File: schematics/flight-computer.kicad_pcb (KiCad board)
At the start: 4 copper layers, 91.4 x 70 mm, 74 parts, among them IC1 NC7SZ04, IC2 MAX14787E, IC3 MAX14787E, J1 BATT, J2 SERIAL, J3 BLACKBOX, J4 BMI-S-201, P1 SWD_TC, P2 GPS, P3 TLM, U1 MAX604, U2 MAX604, U3 STM32F405RGT6, U5 MS5611-01BA, U6 ICM-20948, U7 Si4463, U8 MAX-M8Q, U9 CDCLVC1103PW, Y1 TCXO

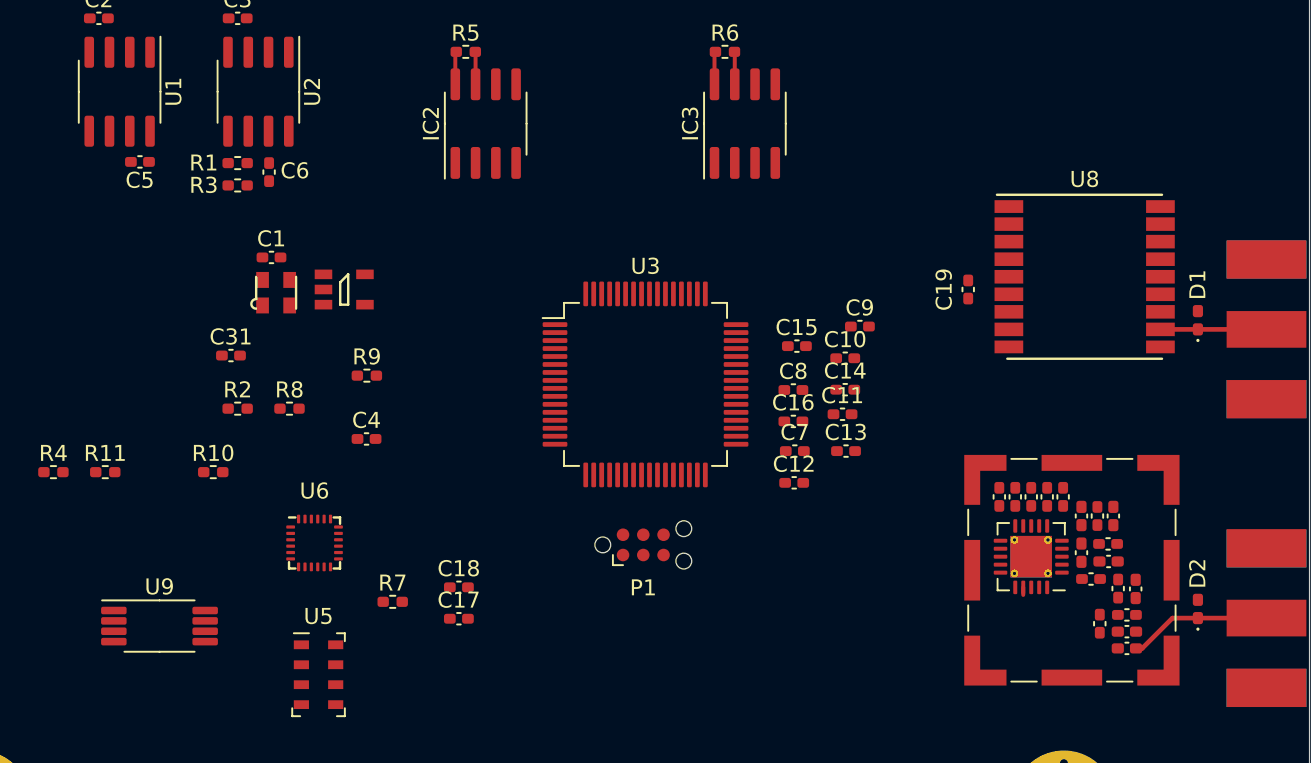
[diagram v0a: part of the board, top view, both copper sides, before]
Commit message: Migrate remaining symbols to local library
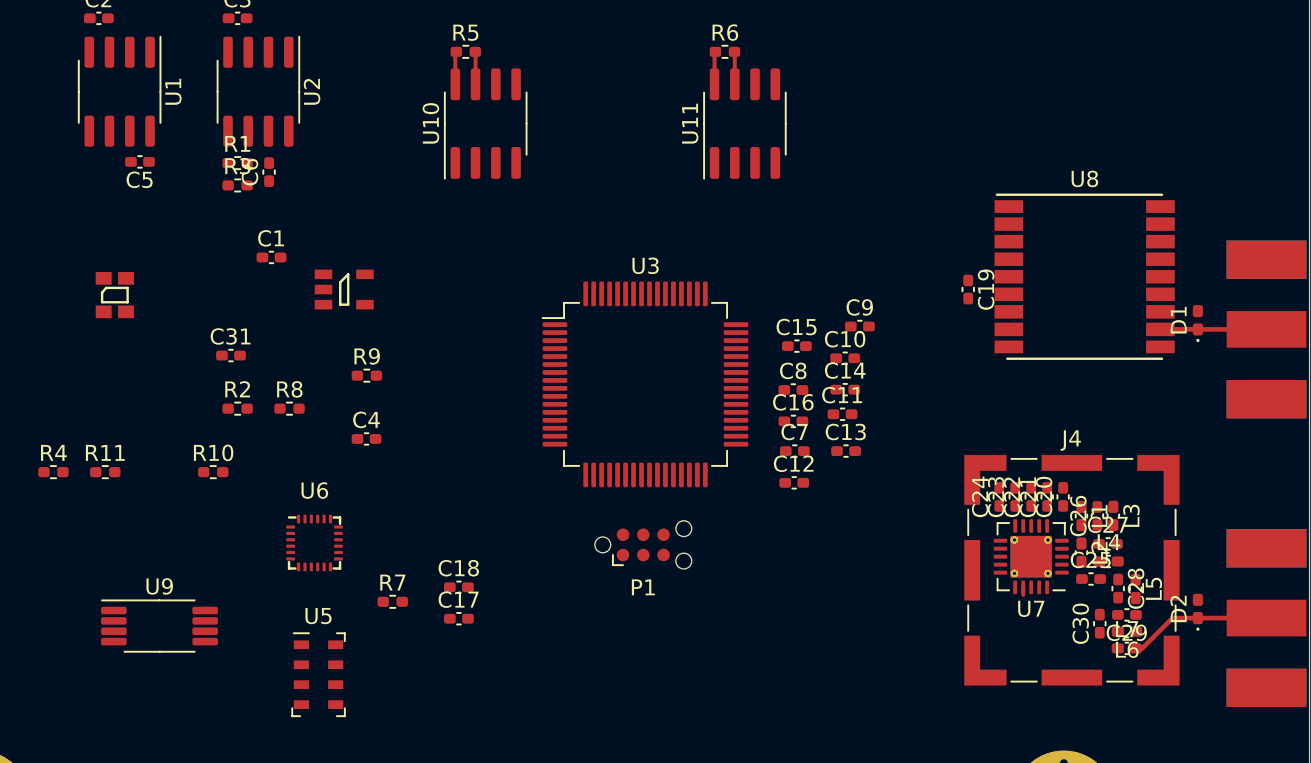
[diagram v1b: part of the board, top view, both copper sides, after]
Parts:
- C1, C10, C11, C12, C13, C14, C15, C16, C17, C18, C19, C2, C20, C21, C22, C23, C24, C25, C26, C27, C28, C29, C3, C30, C31, C4, C5, C6, C7, C8, C9: footprint Strix:C_0402_1005Metric_Pad0.74x0.62mm_HandSolder -> Strix:C_0402
- D1, D2: footprint Strix:D_0402_1005Metric_Pad0.77x0.64mm_HandSolder -> Strix:D_0402
- H1, H2, H3, H4: footprint Strix:MountingHole_3.2mm_M3_Pad_Via -> Strix:MountingHole_Pad
- J1: footprint Strix:Molex_Nano-Fit_105313-xx03_1x03_P2.50mm_Horizontal -> Strix:Molex_Nano-Fit_105313-1103
- J2: footprint Strix:Molex_Nano-Fit_105314-xx06_2x03_P2.50mm_Horizontal -> Strix:Molex_Nano-Fit_105314-1106
- J3: footprint Strix:Molex_Nano-Fit_105314-xx08_2x04_P2.50mm_Horizontal -> Strix:Molex_Nano-Fit_105314-1108
- J4: footprint Strix:Laird_Technologies_BMI-S-201-F_13.66x12.70mm -> Strix:BMI-S-201
- L1, L2, L3, L4, L5, L6, L7: footprint Strix:L_0402_1005Metric_Pad0.77x0.64mm_HandSolder -> Strix:L_0402
- P1: footprint Strix:Tag-Connect_TC2030-IDC-NL_2x03_P1.27mm_Vertical -> Strix:SWD_TC
- R1, R10, R11, R2, R3, R4, R5, R6, R7, R8, R9: footprint Strix:R_0402_1005Metric_Pad0.72x0.64mm_HandSolder -> Strix:R_0402
- U1, U2: footprint Strix:SOIC-8_3.9x4.9mm_P1.27mm -> Strix:MAX604
- U3: footprint Strix:LQFP-64_10x10mm_P0.5mm -> Strix:STM32F405RGT6
- U5: footprint Strix:LGA-8_3x5mm_P1.25mm -> Strix:MS5611-01BA
- U6: footprint Strix:InvenSense_QFN-24_3x3mm_P0.4mm -> Strix:ICM-20948
- U7: footprint Strix:QFN-20-1EP_4x4mm_P0.5mm_EP2.6x2.6mm_ThermalVias -> Strix:Si4463
- U9: footprint Strix:TSSOP-8_4.4x3mm_P0.65mm -> Strix:CDCLVC1103PW
- Y1: value TCXO -> LFTCXO068373; footprint cusf:XTAL-25x20 -> Strix:LFTCXO068373
- moved Y1 10.1 mm to (180.5, 103.2), turned to 0 degrees
- renumbered IC2 to U10, IC3 to U11, IC1 to U12
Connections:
- Y1 pad 1: (no net) -> GND

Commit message: Migrate to KiCad 6
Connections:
- net /BARO_~CS renamed /BARO_~{CS}
- net /GPS_~RESET renamed /GPS_~{RESET}
- net /RADIO_~CS renamed /RADIO_~{CS}
- net /RADIO_~INT renamed /RADIO_~{INT}
- net /~RST renamed /~{RST}
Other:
- net class 50ohm removed
- net class Default removed

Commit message: Complete revision 1 schematic
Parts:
- removed C29, C30: 3p3, Strix:C_0402
- removed C31: 10n, Strix:C_0402
- removed J4: BMI-S-201, Strix:BMI-S-201
- removed P3: TLM, Strix:SMA-EDGE
- removed R10: 10, Strix:R_0402
- removed R11: 10k, Strix:R_0402
- removed R7: 100k, Strix:R_0402
- removed R8, R9: 510k, Strix:R_0402
- removed U10, U11: MAX14787E, Strix:MAX14787E
- removed U12: NC7SZ04, cusf:SOT-23-5
- removed U3: STM32F405RGT6, Strix:STM32F405RGT6
- removed U5: MS5611-01BA, Strix:MS5611-01BA
- removed Y1: LFTCXO068373, Strix:LFTCXO068373
- added U4: MS5611-01BA, Strix:MS5611-01BA, F.Cu at (308.0, 136.0)
- C1: value 100n -> 1µ
- C14: value 2µ2 -> 1u
- C15: value 2µ2 -> 2u2
- C17: value 100n -> 220p
- C18: value 100n -> 100p
- C19: value 100n -> 3p
- C2: value 10u -> 4µ7
- C20: value 1u -> 5p1
- C21: value 2u2 -> 1p2
- C22: value 100n -> 6n8
- C23: value 220p -> 3p3
- C24: value 100p -> 3p3
- C25: value 3p -> 10u
- C26: value 5p1 -> 10u
- C27: value 1p2 -> 10u
- C28: value 6n8 -> 10u
- C3, C5, C6: value 10u -> 100n
- C4: value 1n -> 100n
- C7: value 1µ -> 100n
- C8: value 4µ7 -> 2µ2
- C9: value 100n -> 2µ2
- J2: value SERIAL -> BLACKBOX; footprint Strix:Molex_Nano-Fit_105314-1106 -> Strix:Molex_Nano-Fit_105314-1108
- J3: value BLACKBOX -> BMI-S-201; footprint Strix:Molex_Nano-Fit_105314-1108 -> Strix:BMI-S-201
- P1: value SWD_TC -> GPS; footprint Strix:SWD_TC -> Strix:SMA-EDGE
- P2: value GPS -> TLM
- R1: value 200k -> 120
- R2: value 10 -> 100k
- R3: value 100k -> 10k
- R5: value 120 -> 200k
- R6: value 120 -> 100k
- U1: value MAX604 -> STM32F405RGT6; footprint Strix:MAX604 -> Strix:STM32F405RGT6
- U2: value MAX604 -> MAX14787E; footprint Strix:MAX604 -> Strix:MAX14787E
- U6: value ICM-20948 -> Si4463; footprint Strix:ICM-20948 -> Strix:Si4463
- U7: value Si4463 -> MAX-M8Q; footprint Strix:Si4463 -> Strix:MAX-M8Q
- U8: value MAX-M8Q -> MAX604; footprint Strix:MAX-M8Q -> Strix:MAX604
- U9: value CDCLVC1103PW -> MAX604; footprint Strix:CDCLVC1103PW -> Strix:MAX604
- moved H4 125.9 mm to (262.0, 168.0)
- moved H3 124.5 mm to (328.0, 168.0)
- moved U1 122.6 mm to (295.0, 135.0), turned to 0 degrees
- moved U6 117.4 mm to (310.4, 116.0)
- moved P1 114.4 mm to (323.2, 152.0), turned to -90 degrees
- moved J1 112.6 mm to (266.1, 155.5), turned to 180 degrees
- moved J3 101.8 mm to (312.0, 118.0), turned to 0 degrees
- moved U9 98.7 mm to (276.0, 158.0)
- moved H1 95.9 mm to (262.0, 102.0)
- moved H2 94.0 mm to (328.0, 102.0)
- moved U2 89.8 mm to (275.0, 118.0), turned to 180 degrees
- moved U7 80.8 mm to (312.0, 152.0), turned to 0 degrees
- moved J2 76.3 mm to (268.5, 121.8), turned to 180 degrees
- moved P2 71.6 mm to (323.2, 118.0)
- moved C3 69.2 mm to (237.0, 135.0)
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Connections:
- C1 pad 1: 1v8 -> GND
- C1 pad 2: GND -> 3v3
- C10 pad 2: 3v3 -> /~{RST}
- C11 pad 1: GND -> 3v3
- C11 pad 2: 3v3 -> GND
- C12 pad 1: GND -> 1v8
- C12 pad 2: 3v3 -> unconnected-(C12-Pad2)
- C14 pad 1: GND -> 3v3
- C14 pad 2: Net-(C14-Pad2) -> GND
- C15 pad 1: GND -> 3v3
- C15 pad 2: Net-(C15-Pad2) -> GND
- C16 pad 1: GND -> 3v3
- C16 pad 2: /~{RST} -> GND
- C18 pad 1: 1v8 -> 3v3
- C19 pad 1: GND -> /Radio/RX+
- C19 pad 2: 3v3 -> GND
- C2 pad 1: VBATT -> GND
- C2 pad 2: GND -> 3v3
- C20 pad 1: 3v3 -> /Radio/TX
- C20 pad 2: GND -> Net-(C20-Pad2)
- C21 pad 1: 3v3 -> /Radio/RX-
- C21 pad 2: GND -> Net-(C21-Pad2)
- C22 pad 1: 3v3 -> Net-(C21-Pad2)
- C23 pad 1: 3v3 -> Net-(C23-Pad1)
- C24 pad 1: 3v3 -> Net-(C24-Pad1)
- C25 pad 1: /Radio/RX+ -> VBATT
- C26 pad 1: /Radio/TX -> VBATT
- C26 pad 2: Net-(C26-Pad2) -> GND
- C27 pad 1: /Radio/RX- -> 3v3
- C27 pad 2: Net-(C27-Pad2) -> GND
- C28 pad 1: Net-(C27-Pad2) -> 1v8
- C3 pad 1: VBATT -> GND
- C3 pad 2: GND -> 3v3
- C4 pad 1: Net-(C4-Pad1) -> GND
- C4 pad 2: Net-(C4-Pad2) -> 3v3
- C5 pad 1: 3v3 -> GND
- C5 pad 2: GND -> 3v3
- C6 pad 1: 1v8 -> GND
- C6 pad 2: GND -> 3v3
- C8 pad 2: 3v3 -> Net-(C8-Pad2)
- C9 pad 2: 3v3 -> Net-(C9-Pad2)
- J1 pad 1: VBATT -> /PSU/BATT+
- J1 pad 2: (no net) -> /PSU/BATT_MON
- J1 pad 3: GND -> /PSU/BATT-
- J2 pad 1: /USART1_RX+ -> 3v3
- J2 pad 2: /USART1_RX- -> 3v3
- J2 pad 3: /USART1_TX+ -> /UART4_RX+
- J2 pad 4: /USART1_TX- -> /UART4_RX-
- J2 pad 5: GND -> /UART4_TX+
- J2 pad 6: GND -> /UART4_TX-
- J3 pad 1: 3v3 -> GND
- L3 pad 1: Net-(C26-Pad2) -> Net-(C20-Pad2)
- L3 pad 2: Net-(C27-Pad2) -> Net-(C21-Pad2)
- L4 pad 2: Net-(C27-Pad2) -> Net-(C21-Pad2)
- L5 pad 1: Net-(C27-Pad2) -> Net-(C21-Pad2)
- L5 pad 2: Net-(C29-Pad1) -> Net-(C23-Pad1)
- L6 pad 1: Net-(C29-Pad1) -> Net-(C23-Pad1)
- L6 pad 2: Net-(C30-Pad1) -> Net-(C24-Pad1)
- L7 pad 1: Net-(C30-Pad1) -> Net-(C24-Pad1)
- P1 pad 1: 3v3 -> /Radio/ANT_GPS
- P1 pad 2: /SWDIO -> GND
- P2 pad 1: /Radio/ANT_GPS -> /Radio/ANT_TLM
- R1 pad 1: Net-(R1-Pad1) -> /UART4_RX+
- R1 pad 2: GND -> /UART4_RX-
- R2 pad 1: Net-(R2-Pad1) -> 1v8
- R2 pad 2: /RADIO_CLK -> GND
- R3 pad 1: Net-(R1-Pad1) -> /Radio/RADIO_CLK_1.65V
- R3 pad 2: 1v8 -> /Radio/RADIO_CLK
- R4 pad 2: /RADIO_CLK -> GND
- R5 pad 1: /USART1_RX+ -> Net-(R5-Pad1)
- R5 pad 2: /USART1_RX- -> GND
- R6 pad 1: /UART4_RX+ -> Net-(R5-Pad1)
- R6 pad 2: /UART4_RX- -> 1v8
- U1 pad 1: VBATT -> 3v3
- U1 pad 2: GND -> /BARO_~{CS}
- U1 pad 3: GND -> unconnected-(U1-Pad3)
- U1 pad 4: VBATT -> unconnected-(U1-Pad4)
- U1 pad 5: GND -> /MCU_CLK
- U1 pad 6: GND -> unconnected-(U1-Pad6)
- U1 pad 7: GND -> /~{RST}
- U1 pad 8: 3v3 -> unconnected-(U1-Pad8)
- U2 pad 1: VBATT -> 3v3
- U2 pad 2: GND -> /UART4_RX
- U2 pad 3: GND -> /UART4_TX
- U2 pad 4: VBATT -> GND
- U2 pad 5: Net-(R1-Pad1) -> /UART4_TX+
- U2 pad 6: GND -> /UART4_TX-
- U2 pad 7: GND -> /UART4_RX-
- U2 pad 8: 1v8 -> /UART4_RX+
- U6 pad 1: (no net) -> /RADIO_SDN
- U6 pad 10: GND -> unconnected-(U6-Pad10)
- U6 pad 11: GND -> /RADIO_~{INT}
- U6 pad 12: (no net) -> /SPI2_SCLK
- U6 pad 13: 3v3 -> /SPI2_MISO
- U6 pad 14: (no net) -> /SPI2_MOSI
- U6 pad 15: (no net) -> /RADIO_~{CS}
- U6 pad 16: (no net) -> unconnected-(U6-Pad16)
- U6 pad 17: (no net) -> /Radio/RADIO_CLK_1.65V
- U6 pad 19: (no net) -> unconnected-(U6-Pad19)
- U6 pad 2: (no net) -> /Radio/RX+
- U6 pad 20: GND -> unconnected-(U6-Pad20)
- U6 pad 21: (no net) -> GND
- U6 pad 3: (no net) -> /Radio/RX-
- U6 pad 4: (no net) -> /Radio/TX
- U6 pad 5: (no net) -> unconnected-(U6-Pad5)
- U6 pad 6: (no net) -> 3v3
- U6 pad 7: (no net) -> unconnected-(U6-Pad7)
- U6 pad 8: 1v8 -> 3v3
- U6 pad 9: (no net) -> unconnected-(U6-Pad9)
- U7 pad 1: /RADIO_SDN -> GND
- U7 pad 10: (no net) -> GND
- U7 pad 11: /RADIO_~{INT} -> /Radio/ANT_GPS
- U7 pad 12: /SPI2_SCLK -> GND
- U7 pad 13: /SPI2_MISO -> unconnected-(U7-Pad13)
- U7 pad 14: /SPI2_MOSI -> unconnected-(U7-Pad14)
- U7 pad 15: /RADIO_~{CS} -> unconnected-(U7-Pad15)
- U7 pad 16: (no net) -> unconnected-(U7-Pad16)
- U7 pad 17: /Radio/RADIO_CLK_1.65V -> unconnected-(U7-Pad17)
- U7 pad 18: GND -> unconnected-(U7-Pad18)
- U7 pad 2: /Radio/RX+ -> /USART3_RX
- U7 pad 3: /Radio/RX- -> /USART3_TX
- U7 pad 4: /Radio/TX -> unconnected-(U7-Pad4)
- U7 pad 5: (no net) -> unconnected-(U7-Pad5)
- U7 pad 7: (no net) -> 3v3
- U7 pad 9: (no net) -> /GPS_~{RESET}
- U8 pad 1: GND -> VBATT
- U8 pad 2: /USART3_RX -> GND
- U8 pad 3: /USART3_TX -> GND
- U8 pad 4: (no net) -> VBATT
- U8 pad 5: (no net) -> GND
- U8 pad 6: 3v3 -> GND
- U8 pad 7: 3v3 -> GND
- U9 pad 1: Net-(R9-Pad2) -> VBATT
- U9 pad 2: 3v3 -> GND
- U9 pad 3: Net-(R10-Pad1) -> GND
- U9 pad 4: GND -> VBATT
- U9 pad 5: (no net) -> Net-(R5-Pad1)
- U9 pad 6: 3v3 -> GND
- U9 pad 7: (no net) -> GND
- U9 pad 8: Net-(R2-Pad1) -> 1v8
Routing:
- net /Radio/ANT_TLM: track 8.96 -> 0.00 mm
- net /Radio/ANT_GPS: track 6.65 -> 0.00 mm
- net /USART1_RX+: track 2.06 -> 0.00 mm
- net /UART4_RX+: track 2.06 -> 0.00 mm
- net /USART1_RX-: track 2.04 -> 0.00 mm
- net /UART4_RX-: track 2.04 -> 0.00 mm
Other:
- board size 91.4 x 70 mm -> 80 x 80 mm
- board text removed: "Christ, what an imagination I’ve got!"
